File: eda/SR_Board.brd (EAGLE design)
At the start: 101.6 x 81.3 mm, 18 parts

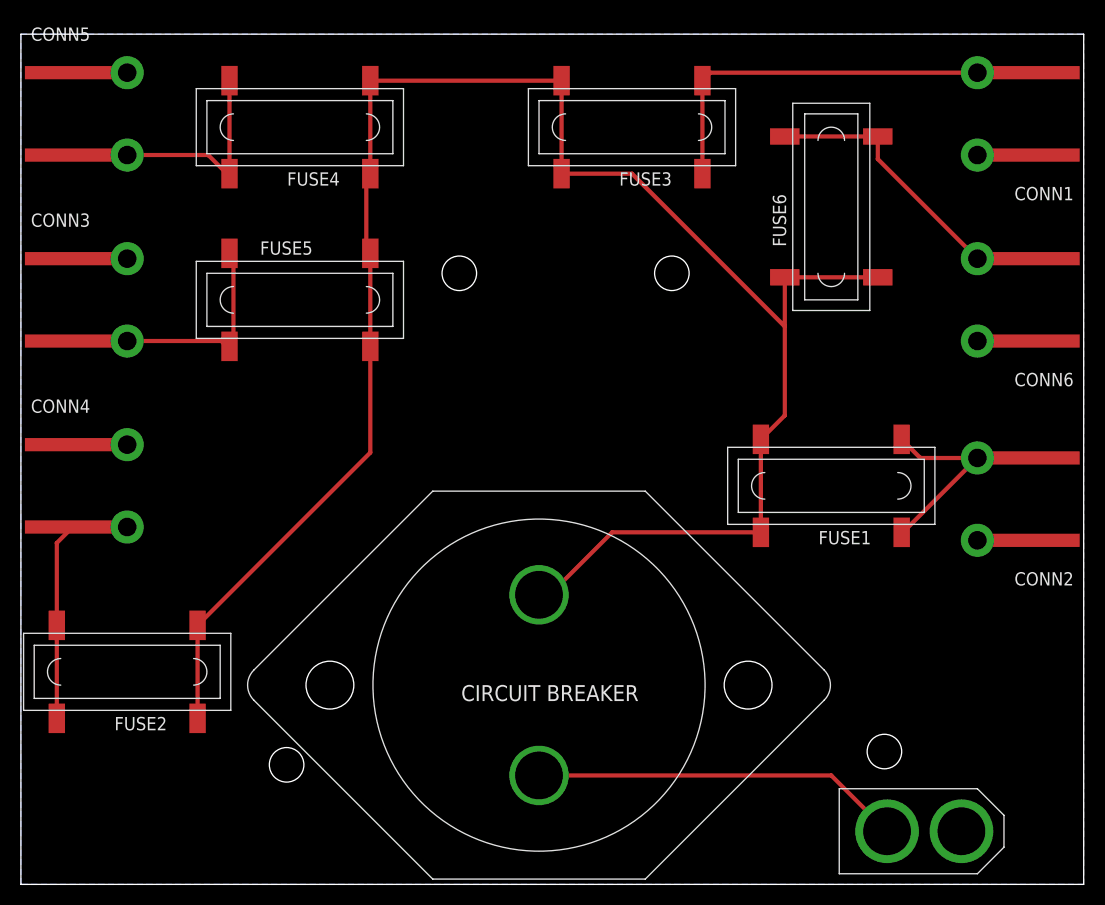
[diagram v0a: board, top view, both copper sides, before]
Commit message: Eliminated Overlaps
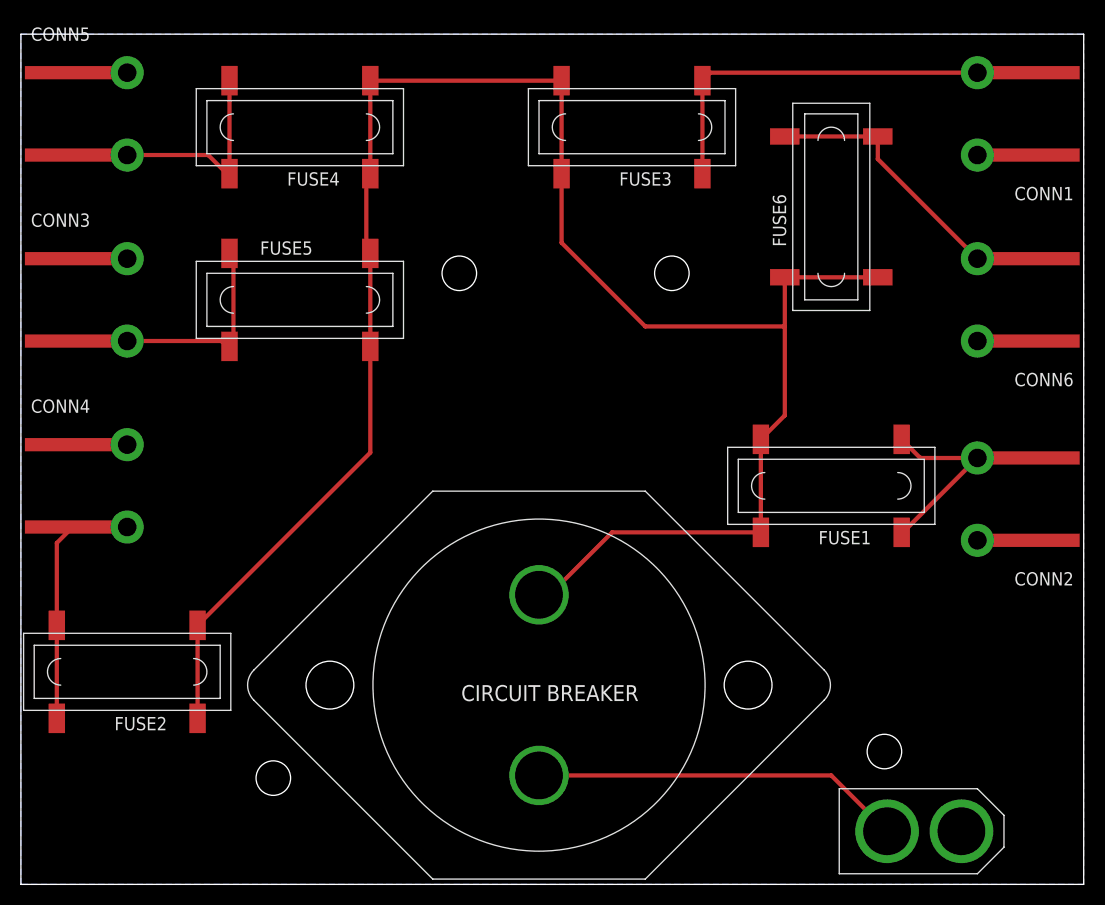
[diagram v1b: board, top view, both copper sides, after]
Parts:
- moved U$2 1.80 mm to (24.1, 10.2)
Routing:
- net 12V: track 186.4 -> 190.2 mm
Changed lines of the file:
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@@
 <attribute name="PIE-INT-REF-NUM" value="Anderson" x="91.44" y="55.88" size="1.778" layer="27" rot="R180" display="off"/>
 </element>
-<element name="U$2" library="pie" package="STAND-OFF" value="" x="25.4" y="11.43"/>
+<element name="U$2" library="pie" package="STAND-OFF" value="" x="24.13" y="10.16"/>
 <element name="U$3" library="pie" package="STAND-OFF" value="" x="41.91" y="58.42"/>
 <element name="U$4" library="pie" package="STAND-OFF" value="" x="62.23" y="58.42"/>
@@
 <wire x1="70.739" y1="33.655" x2="56.515" y2="33.655" width="0.4064" layer="1"/>
 <wire x1="56.515" y1="33.655" x2="49.53" y2="26.67" width="0.4064" layer="1"/>
-<wire x1="51.689" y1="67.945" x2="58.42" y2="67.945" width="0.4064" layer="1"/>
-<wire x1="58.42" y1="67.945" x2="73.025" y2="53.34" width="0.4064" layer="1"/>
 <wire x1="51.689" y1="67.945" x2="51.689" y2="75.819" width="0.4064" layer="1"/>
 <wire x1="51.689" y1="75.819" x2="52.07" y2="76.2" width="0.4064" layer="1"/>
@@
 <wire x1="16.891" y1="24.765" x2="16.891" y2="15.875" width="0.4064" layer="1"/>
 <wire x1="49.53" y1="26.67" x2="49.53" y2="27.686" width="0.4064" layer="1"/>
+<wire x1="51.689" y1="67.945" x2="51.689" y2="61.341" width="0.4064" layer="1"/>
+<wire x1="51.689" y1="61.341" x2="59.69" y2="53.34" width="0.4064" layer="1"/>
+<wire x1="59.69" y1="53.34" x2="73.025" y2="53.34" width="0.4064" layer="1"/>
 </signal>
 <signal name="N$1">

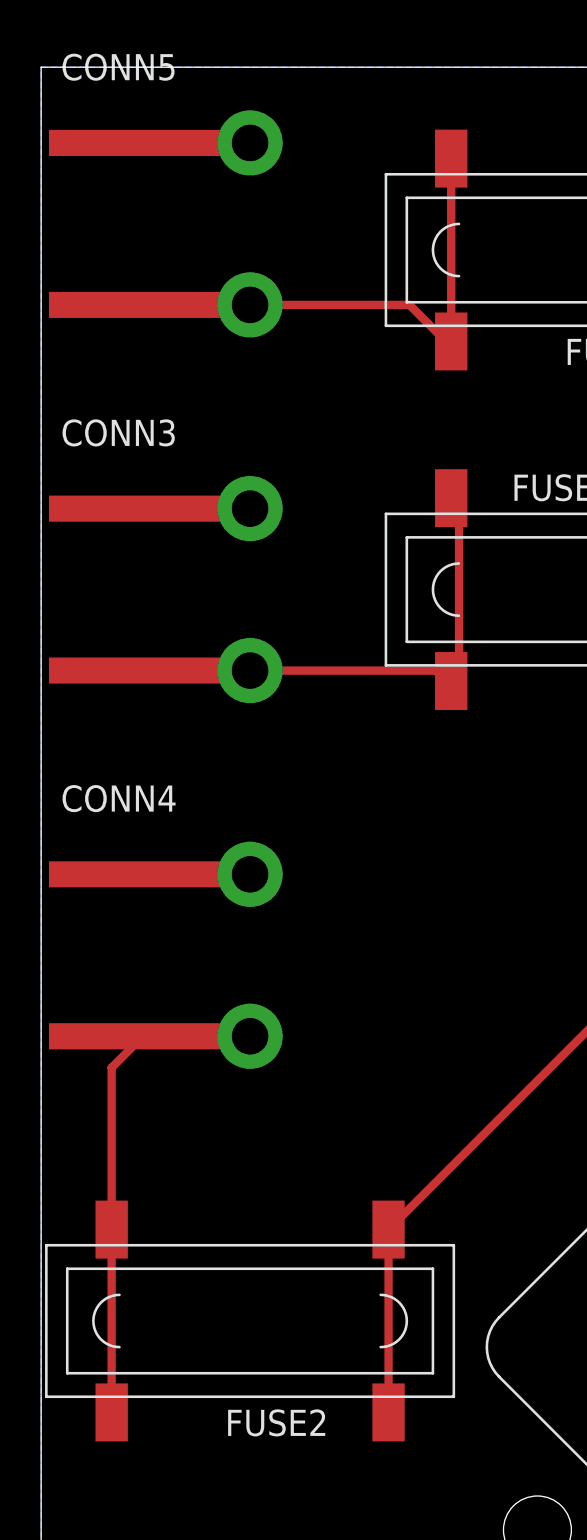
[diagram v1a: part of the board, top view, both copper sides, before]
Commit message: Moved Fuses so Conn5 No longer falls outside boundaries of frame.
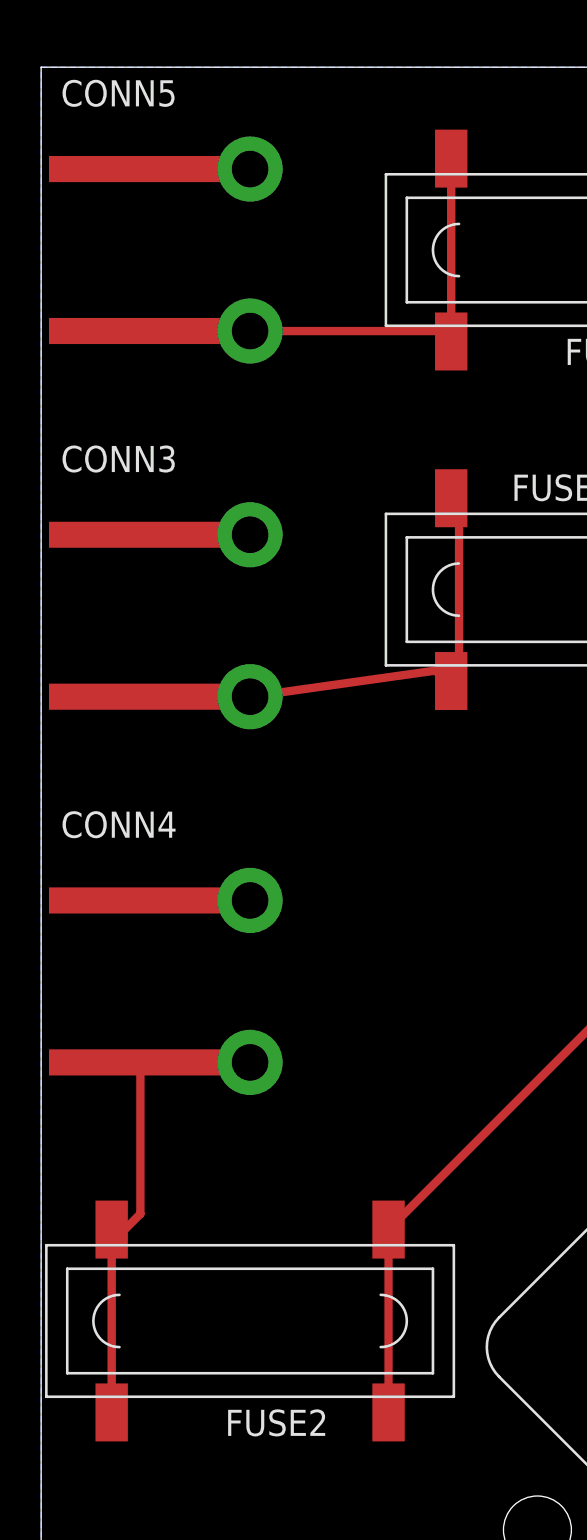
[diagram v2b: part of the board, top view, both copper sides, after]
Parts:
- moved CONN3 1.27 mm to (10.2, 54.6)
- moved CONN4 1.27 mm to (10.2, 36.8)
- moved CONN5 1.27 mm to (10.2, 72.4)
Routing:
- net N$5: track 29.6 -> 23.6 mm
- net N$2: track 28.3 -> 26.3 mm
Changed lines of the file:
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@@
 <attribute name="PIE-INT-REF-NUM" value="Anderson" x="91.44" y="36.83" size="1.778" layer="27" rot="R180" display="off"/>
 </element>
-<element name="CONN4" library="pie" package="ANDERSON_HORIZONTAL" value="ANDERSONHORIZONTAL" x="10.16" y="38.1">
-<attribute name="PIE-INT-REF-NUM" value="Anderson" x="10.16" y="38.1" size="1.778" layer="27" display="off"/>
-</element>
-<element name="CONN5" library="pie" package="ANDERSON_HORIZONTAL" value="ANDERSONHORIZONTAL" x="10.16" y="73.66">
-<attribute name="PIE-INT-REF-NUM" value="Anderson" x="10.16" y="73.66" size="1.778" layer="27" display="off"/>
+<element name="CONN4" library="pie" package="ANDERSON_HORIZONTAL" value="ANDERSONHORIZONTAL" x="10.16" y="36.83">
+<attribute name="PIE-INT-REF-NUM" value="Anderson" x="10.16" y="36.83" size="1.778" layer="27" display="off"/>
+</element>
+<element name="CONN5" library="pie" package="ANDERSON_HORIZONTAL" value="ANDERSONHORIZONTAL" x="10.16" y="72.39">
+<attribute name="PIE-INT-REF-NUM" value="Anderson" x="10.16" y="72.39" size="1.778" layer="27" display="off"/>
 </element>
 <element name="U$1" library="pie" package="XT60CONNECTOR" value="XT60CONNECTOR" x="86.36" y="5.08">
@@
 <attribute name="MANUF-PN" value="3587" x="77.47" y="64.77" size="1.778" layer="27" rot="R90" display="off"/>
 </element>
-<element name="CONN3" library="pie" package="ANDERSON_HORIZONTAL" value="ANDERSONHORIZONTAL" x="10.16" y="55.88">
-<attribute name="PIE-INT-REF-NUM" value="Anderson" x="10.16" y="55.88" size="1.778" layer="27" display="off"/>
+<element name="CONN3" library="pie" package="ANDERSON_HORIZONTAL" value="ANDERSONHORIZONTAL" x="10.16" y="54.61">
+<attribute name="PIE-INT-REF-NUM" value="Anderson" x="10.16" y="54.61" size="1.778" layer="27" display="off"/>
 </element>
 <element name="CONN6" library="pie" package="ANDERSON_HORIZONTAL" value="ANDERSONHORIZONTAL" x="91.44" y="55.88" rot="R180">
@@
 <wire x1="97.79" y1="52.07" x2="96.901" y2="52.07" width="0.4064" layer="1"/>
 <wire x1="96.901" y1="52.07" x2="96.774" y2="51.943" width="0.4064" layer="1"/>
-<wire x1="10.16" y1="77.597" x2="4.826" y2="77.597" width="0.4064" layer="1"/>
-<wire x1="10.16" y1="59.817" x2="5.207" y2="59.817" width="0.4064" layer="1"/>
-<wire x1="5.207" y1="59.817" x2="5.08" y2="59.69" width="0.4064" layer="1"/>
-<wire x1="5.08" y1="59.69" x2="4.953" y2="59.69" width="0.4064" layer="1"/>
-<wire x1="4.953" y1="59.69" x2="4.826" y2="59.817" width="0.4064" layer="1"/>
 <wire x1="91.44" y1="32.893" x2="96.774" y2="32.893" width="0.4064" layer="1"/>
+<wire x1="4.826" y1="58.547" x2="10.16" y2="58.547" width="0.4064" layer="1"/>
+<wire x1="4.826" y1="76.327" x2="10.16" y2="76.327" width="0.4064" layer="1"/>
 </signal>
 <signal name="12V">
@@
 <contactref element="FUSE2" pad="P$2_UP"/>
 <contactref element="FUSE2" pad="P$2_DOWN"/>
-<wire x1="10.16" y1="34.163" x2="4.826" y2="34.163" width="0.4064" layer="1"/>
-<wire x1="3.429" y1="15.875" x2="3.429" y2="24.765" width="0.4064" layer="1"/>
-<wire x1="3.429" y1="24.765" x2="3.429" y2="32.639" width="0.4064" layer="1"/>
-<wire x1="3.429" y1="32.639" x2="5.08" y2="34.29" width="0.4064" layer="1"/>
-<wire x1="5.08" y1="34.29" x2="10.033" y2="34.29" width="0.4064" layer="1"/>
-<wire x1="10.033" y1="34.29" x2="10.16" y2="34.163" width="0.4064" layer="1"/>
+<wire x1="3.429" y1="15.875" x2="3.429" y2="24.13" width="0.4064" layer="1"/>
+<wire x1="3.429" y1="24.13" x2="3.429" y2="24.765" width="0.4064" layer="1"/>
+<wire x1="10.16" y1="32.893" x2="4.826" y2="32.893" width="0.4064" layer="1"/>
+<wire x1="4.826" y1="32.893" x2="4.826" y2="25.527" width="0.4064" layer="1"/>
+<wire x1="4.826" y1="25.527" x2="3.429" y2="24.13" width="0.4064" layer="1"/>
 </signal>
 <signal name="N$6">
 <contactref element="CONN4" pad="PIN1"/>
 <contactref element="CONN4" pad="PIN1-LEAD"/>
-<wire x1="10.16" y1="42.037" x2="4.826" y2="42.037" width="0.4064" layer="1"/>
+<wire x1="10.16" y1="40.767" x2="4.826" y2="40.767" width="0.4064" layer="1"/>
 </signal>
 <signal name="N$2">
@@
 <contactref element="CONN5" pad="PIN2-LEAD"/>
 <wire x1="20.32" y1="76.454" x2="19.939" y2="76.835" width="0.4064" layer="1"/>
-<wire x1="10.16" y1="69.723" x2="17.907" y2="69.723" width="0.4064" layer="1"/>
-<wire x1="17.907" y1="69.723" x2="20.32" y2="67.31" width="0.4064" layer="1"/>
-<wire x1="20.32" y1="67.31" x2="20.32" y2="67.564" width="0.4064" layer="1"/>
-<wire x1="20.32" y1="67.564" x2="19.939" y2="67.945" width="0.4064" layer="1"/>
 <wire x1="19.939" y1="67.945" x2="19.939" y2="76.835" width="0.4064" layer="1"/>
 <wire x1="19.939" y1="76.835" x2="19.939" y2="77.089" width="0.4064" layer="1"/>
@@
 <wire x1="20.32" y1="77.47" x2="20.32" y2="77.216" width="0.4064" layer="1"/>
 <wire x1="20.32" y1="77.216" x2="19.939" y2="76.835" width="0.4064" layer="1"/>
-<wire x1="10.16" y1="69.723" x2="4.826" y2="69.723" width="0.4064" layer="1"/>
+<wire x1="10.16" y1="68.453" x2="19.431" y2="68.453" width="0.4064" layer="1"/>
+<wire x1="19.431" y1="68.453" x2="19.939" y2="67.945" width="0.4064" layer="1"/>
+<wire x1="10.16" y1="68.453" x2="4.826" y2="68.453" width="0.4064" layer="1"/>
 </signal>
 <signal name="N$4">
@@
 <contactref element="CONN3" pad="PIN2"/>
 <contactref element="CONN3" pad="PIN2-LEAD"/>
-<wire x1="4.826" y1="51.943" x2="10.16" y2="51.943" width="0.4064" layer="1"/>
+<wire x1="4.826" y1="50.673" x2="10.16" y2="50.673" width="0.4064" layer="1"/>
 <wire x1="20.32" y1="50.8" x2="20.32" y2="59.944" width="0.4064" layer="1"/>
 <wire x1="20.32" y1="59.944" x2="19.939" y2="60.325" width="0.4064" layer="1"/>
-<wire x1="10.16" y1="51.943" x2="19.177" y2="51.943" width="0.4064" layer="1"/>
+<wire x1="10.16" y1="50.673" x2="19.177" y2="51.943" width="0.4064" layer="1"/>
 <wire x1="19.177" y1="51.943" x2="19.939" y2="51.181" width="0.4064" layer="1"/>
 <wire x1="19.939" y1="51.435" x2="19.939" y2="51.181" width="0.4064" layer="1"/>

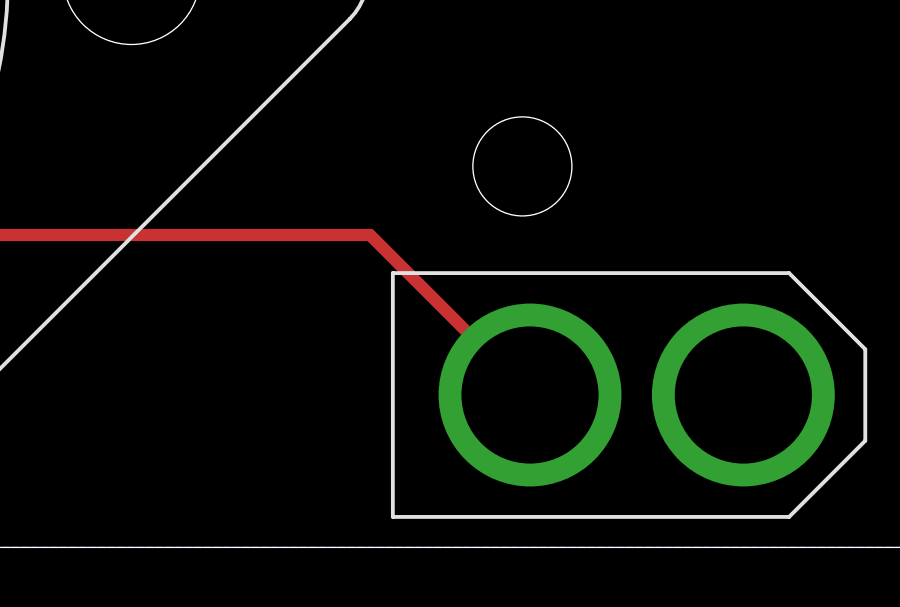
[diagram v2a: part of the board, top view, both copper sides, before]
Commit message: Moved Frame to origin. Replaced GND with GND from Pi library.
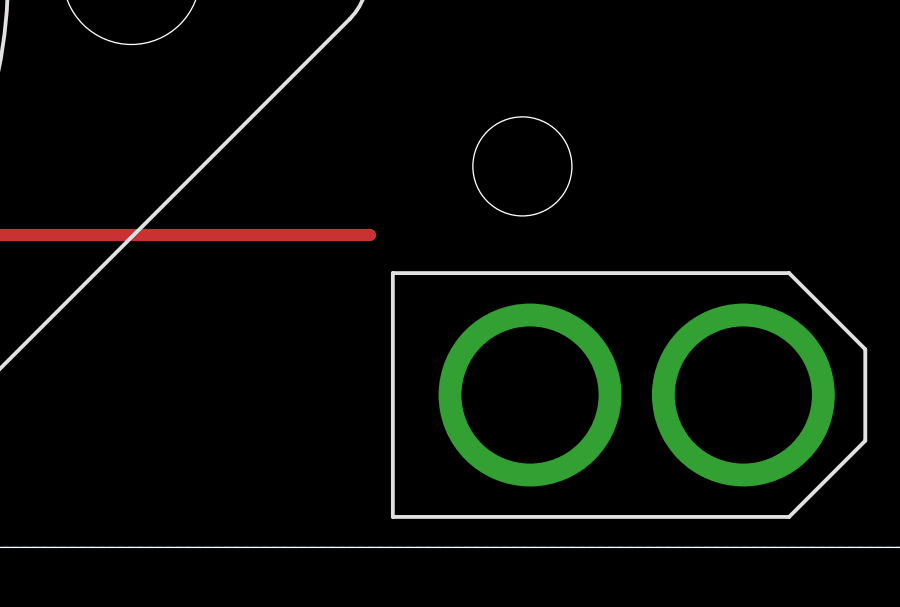
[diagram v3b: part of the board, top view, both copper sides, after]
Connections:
- removed net N$6: CONN4.PIN1, CONN4.PIN1-LEAD
- removed net N$8: CONN1.PIN1, CONN1.PIN1-LEAD
- net GND: now also CONN1.PIN1, CONN1.PIN1-LEAD, CONN4.PIN1, CONN4.PIN1-LEAD
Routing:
- net GND: track 23.5 -> 34.1 mm
- net BAT: track 35.5 -> 27.9 mm
- net N$8: track 5.33 -> 0.00 mm
- net N$6: track 5.33 -> 0.00 mm
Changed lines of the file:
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@@
 <signals>
 <signal name="GND">
-<contactref element="U$1" pad="GND"/>
-<contactref element="CONN2" pad="PIN1"/>
-<contactref element="CONN2" pad="PIN1-LEAD"/>
-<contactref element="CONN5" pad="PIN1"/>
-<contactref element="CONN5" pad="PIN1-LEAD"/>
-<contactref element="CONN3" pad="PIN1"/>
-<contactref element="CONN3" pad="PIN1-LEAD"/>
-<contactref element="CONN6" pad="PIN1"/>
-<contactref element="CONN6" pad="PIN1-LEAD"/>
 <polygon width="0.4064" layer="16">
 <vertex x="0" y="81.28"/>
@@
 <vertex x="0" y="0"/>
 </polygon>
+<contactref element="U$1" pad="GND"/>
+<contactref element="CONN2" pad="PIN1"/>
+<contactref element="CONN2" pad="PIN1-LEAD"/>
+<wire x1="91.44" y1="32.893" x2="96.774" y2="32.893" width="0.4064" layer="1"/>
+<contactref element="CONN4" pad="PIN1"/>
+<contactref element="CONN4" pad="PIN1-LEAD"/>
+<wire x1="10.16" y1="40.767" x2="4.826" y2="40.767" width="0.4064" layer="1"/>
+<contactref element="CONN1" pad="PIN1"/>
+<contactref element="CONN1" pad="PIN1-LEAD"/>
+<wire x1="91.44" y1="69.723" x2="96.774" y2="69.723" width="0.4064" layer="1"/>
+<contactref element="CONN5" pad="PIN1"/>
+<contactref element="CONN5" pad="PIN1-LEAD"/>
+<wire x1="4.826" y1="76.327" x2="10.16" y2="76.327" width="0.4064" layer="1"/>
+<contactref element="CONN3" pad="PIN1"/>
+<contactref element="CONN3" pad="PIN1-LEAD"/>
+<wire x1="4.826" y1="58.547" x2="10.16" y2="58.547" width="0.4064" layer="1"/>
+<contactref element="CONN6" pad="PIN1"/>
+<contactref element="CONN6" pad="PIN1-LEAD"/>
 <wire x1="91.44" y1="51.943" x2="96.774" y2="51.943" width="0.4064" layer="1"/>
 <wire x1="96.774" y1="51.943" x2="97.663" y2="51.943" width="0.4064" layer="1"/>
@@
 <wire x1="97.79" y1="52.07" x2="96.901" y2="52.07" width="0.4064" layer="1"/>
 <wire x1="96.901" y1="52.07" x2="96.774" y2="51.943" width="0.4064" layer="1"/>
-<wire x1="91.44" y1="32.893" x2="96.774" y2="32.893" width="0.4064" layer="1"/>
-<wire x1="4.826" y1="58.547" x2="10.16" y2="58.547" width="0.4064" layer="1"/>
-<wire x1="4.826" y1="76.327" x2="10.16" y2="76.327" width="0.4064" layer="1"/>
+<wire x1="96.901" y1="52.07" x2="96.774" y2="69.723" width="0" layer="19" extent="1-1"/>
+<wire x1="96.774" y1="32.893" x2="97.663" y2="51.943" width="0" layer="19" extent="1-1"/>
+<wire x1="89.916" y1="5.08" x2="91.44" y2="32.893" width="0" layer="19" extent="1-1"/>
+<wire x1="10.16" y1="76.327" x2="91.44" y2="69.723" width="0" layer="19" extent="1-1"/>
+<wire x1="10.16" y1="58.547" x2="10.16" y2="76.327" width="0" layer="19" extent="1-1"/>
+<wire x1="10.16" y1="40.767" x2="10.16" y2="58.547" width="0" layer="19" extent="1-1"/>
 </signal>
 <signal name="12V">
@@
 <wire x1="91.44" y1="77.597" x2="96.774" y2="77.597" width="0.4064" layer="1"/>
 </signal>
-<signal name="N$8">
-<contactref element="CONN1" pad="PIN1"/>
-<contactref element="CONN1" pad="PIN1-LEAD"/>
-<wire x1="91.44" y1="69.723" x2="96.774" y2="69.723" width="0.4064" layer="1"/>
-</signal>
 <signal name="N$5">
 <contactref element="CONN4" pad="PIN2"/>
@@
 <wire x1="4.826" y1="32.893" x2="4.826" y2="25.527" width="0.4064" layer="1"/>
 <wire x1="4.826" y1="25.527" x2="3.429" y2="24.13" width="0.4064" layer="1"/>
-</signal>
-<signal name="N$6">
-<contactref element="CONN4" pad="PIN1"/>
-<contactref element="CONN4" pad="PIN1-LEAD"/>
-<wire x1="10.16" y1="40.767" x2="4.826" y2="40.767" width="0.4064" layer="1"/>
 </signal>
 <signal name="N$2">
@@
 </signal>
 <signal name="BAT">
-<contactref element="U$1" pad="12V"/>
 <contactref element="CIRCUIT_BREAKER" pad="P$1"/>
 <wire x1="49.53" y1="10.414" x2="77.47" y2="10.414" width="0.4064" layer="1"/>
-<wire x1="77.47" y1="10.414" x2="82.804" y2="5.08" width="0.4064" layer="1"/>
+<contactref element="U$1" pad="12V"/>
+<wire x1="77.47" y1="10.414" x2="82.804" y2="5.08" width="0" layer="19" extent="1-1"/>
 </signal>
 </signals>
